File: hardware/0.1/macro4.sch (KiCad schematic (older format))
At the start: 22 parts, among them J1 USB_C_Receptacle_USB2.0, SW1 DFU, SW2 RST, SW3 SW_Push, SW5 SW_Push, SW6 SW_Push, SW7 Rotary_Encoder_MX, U1 AP2112K-3.3, U2 STM32F072C8Tx

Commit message: add RGB and silk to macro4
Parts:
- removed C6, C7: 100n, Capacitor_SMD:C_0603_1608Metric, symbol Device:C
- removed RN2: 10K, Resistor_SMD:R_Array_Convex_4x0603, symbol josh-passive:RN
- added D1, D2, D3: WS2812B, LED_SMD:LED_WS2812B_PLCC4_5.0x5.0mm_P3.2mm, symbol LED:WS2812B
- added Q1: BSS138, Package_TO_SOT_SMD:SOT-23, symbol Transistor_FET:BSS138
- added R1, R2: 10K, Resistor_SMD:R_0603_1608Metric_Pad1.05x0.95mm_HandSolder, symbol Device:R
- C1, C3: LCSC PN (none) -> C15849; MPN (none) -> CL10A105KB8NNNC
- C2, C4, C5: LCSC PN (none) -> C14663; MPN (none) -> CC0603KRX7R9BB104
- H1, H2, H3, H4, SW7: DNP (none) -> DNP
- J1: LCSC PN (none) -> C319148; MPN (none) -> U262-161N-4BVC11
- RN1: LCSC PN (none) -> C12028; MPN (none) -> 4D03WGJ0512T5E
- SW1, SW2: LCSC PN (none) -> C318936; MPN (none) -> TS-1101VS-C-A-A
- SW3, SW5, SW6: value SW_Push -> CHERRY_MX; DNP (none) -> DNP
- U1: LCSC PN (none) -> C51118; MPN (none) -> AP2112K-3.3TRG1
- U2: LCSC PN (none) -> C80488; MPN (none) -> STM32F072C8T6
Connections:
- net +3V3: now also Q1.1 (G), R1.1
- net ENC_A: now also SW7.A, U2.41 (PB5); no longer U2.42 (PB6)
- net ENC_B: now also SW7.B, U2.42 (PB6); no longer U2.41 (PB5)
- net GND: now also D1.3 (VSS), D2.3 (VSS), D3.3 (VSS)
- net VBUS: now also D1.1 (VDD), D2.1 (VDD), D3.1 (VDD), R2.1
- net LED: now reaches U2.25 (PB12)
- net LED: now also Q1.2 (S), R1.2
- new net: D1.2 (DOUT), D2.4 (DIN)
- new net: D1.4 (DIN), Q1.3 (D), R2.2
- new net: D2.2 (DOUT), D3.4 (DIN)
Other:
- note added: "Note: Encoder can be a MX switch or an encoder."
- note added: "Stopping ERC Errors"
- note removed: "Note: Encoder can be a MX switch or an encoder.\nOnly populate one!"
- note removed: "Stopping ERC"
- moved on the sheet: C2, H1, H2, H3, H4, RN1C, RN1D, SW1, SW2, SW7

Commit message: change buttons
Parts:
- SW1, SW2: footprint josh-buttons-switches:TL3330AF130QG -> josh-buttons-switches:Panasonic_EVQPUL_EVQPUC
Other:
- note added: "3v3 -> 5v logic shift"
- note added: "Addressable LEDs"
- moved on the sheet: D1, D2, D3, Q1, R1, R2, SW7

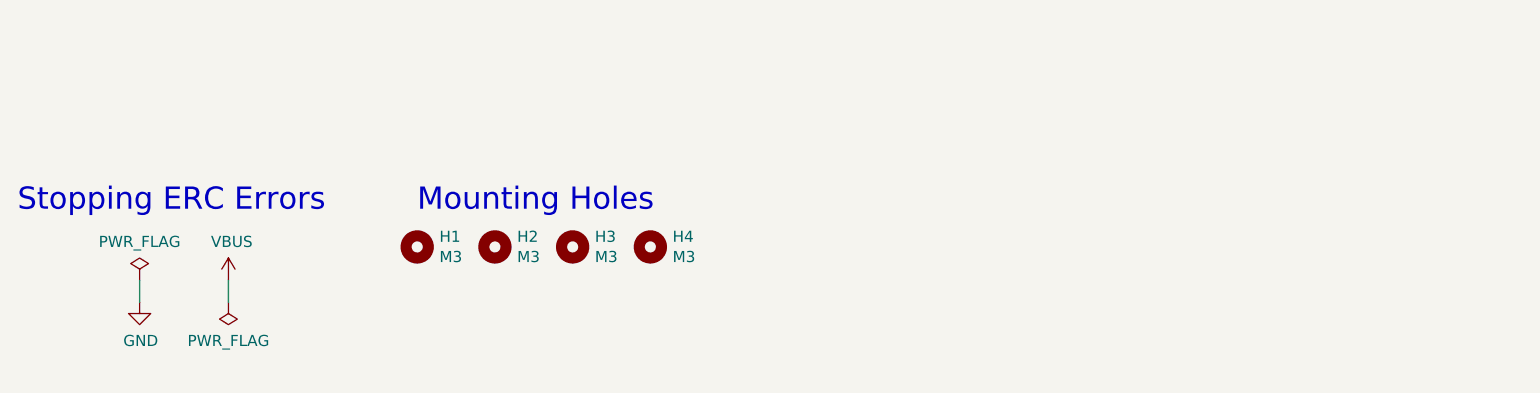
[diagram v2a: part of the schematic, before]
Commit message: update due to breaking lib change
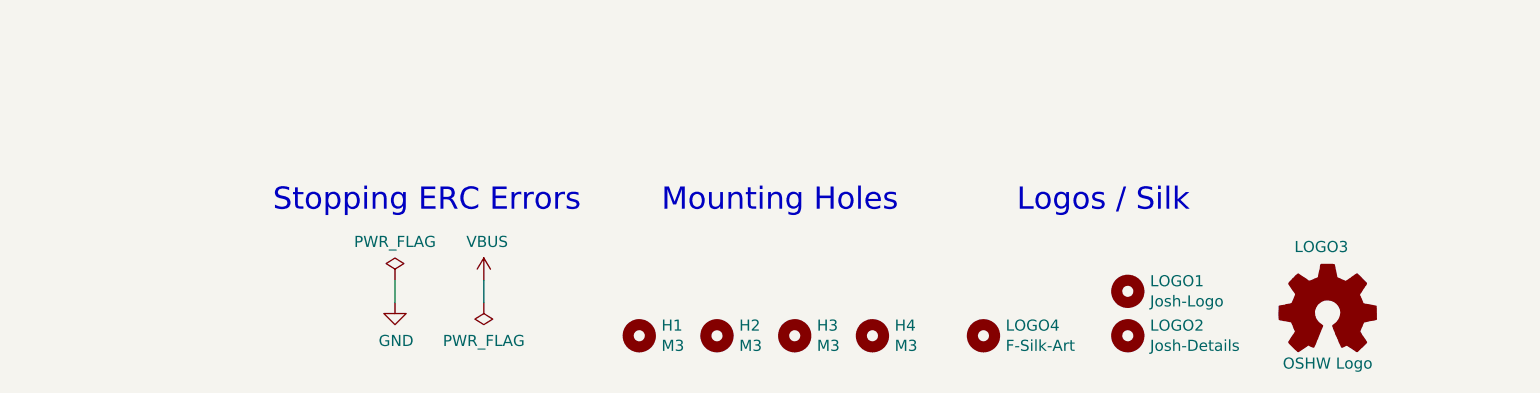
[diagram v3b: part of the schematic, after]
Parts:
- added LOGO1: Josh-Logo, josh-logos:josh-johnson-logo-11x2, symbol Mechanical:MountingHole
- added LOGO2: Josh-Details, josh-logos:josh-details, symbol Mechanical:MountingHole
- added LOGO3: OSHW Logo, josh-logos:OSHW_Logo_3.6x3.6_F.Mask, symbol Graphic:Logo_Open_Hardware_Small
- added LOGO4: F-Silk-Art, art:pattern_top, symbol Mechanical:MountingHole
- J1: footprint josh-connectors:USB_C_Receptacle_GT-USB-7010 -> josh-connectors:USB_C_U262-161N-4BVC11
- SW1, SW2: footprint josh-buttons-switches:Panasonic_EVQPUL_EVQPUC -> josh-buttons-switches:SW_Push_EVQPUL_EVQPUC
- SW3, SW5, SW6: footprint josh-buttons-switches:SW_Cherry_MX_1.00u_PCB -> josh-keyboard:MX_KEYSWITCH
- SW7: footprint josh-buttons-switches:MX_KEYSWITCH_ENCODER -> josh-keyboard:MX_KEYSWITCH_ENCODER
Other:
- note added: "Logos / Silk"
- moved on the sheet: H1, H2, H3, H4
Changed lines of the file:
@@
 F 0 "J1" H 950 3000 50  0000 C CNN
 F 1 "USB_C_Receptacle_USB2.0" H 1407 2926 50  0000 C CNN
-F 2 "josh-connectors:USB_C_Receptacle_GT-USB-7010" H 1450 2150 50  0001 C CNN
+F 2 "josh-connectors:USB_C_U262-161N-4BVC11" H 1450 2150 50  0001 C CNN
 F 3 "https://www.usb.org/sites/default/files/documents/usb_type-c.zip" H 1450 2150 50  0001 C CNN
 F 4 "C319148" H 1300 2150 50  0001 C CNN "LCSC PN"
@@
 F 0 "SW1" V 8696 3952 50  0000 R CNN
 F 1 "DFU" V 8605 3952 50  0000 R CNN
-F 2 "josh-buttons-switches:Panasonic_EVQPUL_EVQPUC" H 8650 4200 50  0001 C CNN
+F 2 "josh-buttons-switches:SW_Push_EVQPUL_EVQPUC" H 8650 4200 50  0001 C CNN
 F 3 "~" H 8650 4200 50  0001 C CNN
 F 4 "C318936" H 8650 4000 50  0001 C CNN "LCSC PN"
@@
 F 0 "SW2" V 9996 4402 50  0000 R CNN
 F 1 "RST" V 9905 4402 50  0000 R CNN
-F 2 "josh-buttons-switches:Panasonic_EVQPUL_EVQPUC" H 9950 4650 50  0001 C CNN
+F 2 "josh-buttons-switches:SW_Push_EVQPUL_EVQPUC" H 9950 4650 50  0001 C CNN
 F 3 "~" H 9950 4650 50  0001 C CNN
 F 4 "C318936" H 9950 4450 50  0001 C CNN "LCSC PN"
@@
 F 0 "SW7" H 9100 2367 50  0000 C CNN
 F 1 "Rotary_Encoder_MX" H 9100 2276 50  0000 C CNN
-F 2 "josh-buttons-switches:MX_KEYSWITCH_ENCODER" H 8950 2160 50  0001 C CNN
+F 2 "josh-keyboard:MX_KEYSWITCH_ENCODER" H 8950 2160 50  0001 C CNN
 F 3 "~" H 9100 2260 50  0001 C CNN
 F 4 "DNP" H 9100 2000 50  0001 C CNN "DNP"
@@
 F 0 "SW3" H 7600 2135 50  0000 C CNN
 F 1 "CHERRY_MX" H 7600 2044 50  0000 C CNN
-F 2 "josh-buttons-switches:SW_Cherry_MX_1.00u_PCB" H 7600 2050 50  0001 C CNN
+F 2 "josh-keyboard:MX_KEYSWITCH" H 7600 2050 50  0001 C CNN
 F 3 "~" H 7600 2050 50  0001 C CNN
 F 4 "DNP" H 7600 1850 50  0001 C CNN "DNP"
@@
 F 0 "SW5" H 7600 2535 50  0000 C CNN
 F 1 "CHERRY_MX" H 7600 2444 50  0000 C CNN
-F 2 "josh-buttons-switches:SW_Cherry_MX_1.00u_PCB" H 7600 2450 50  0001 C CNN
+F 2 "josh-keyboard:MX_KEYSWITCH" H 7600 2450 50  0001 C CNN
 F 3 "~" H 7600 2450 50  0001 C CNN
 F 4 "DNP" H 7600 2250 50  0001 C CNN "DNP"
@@
 F 0 "SW6" H 7600 2935 50  0000 C CNN
 F 1 "CHERRY_MX" H 7600 2844 50  0000 C CNN
-F 2 "josh-buttons-switches:SW_Cherry_MX_1.00u_PCB" H 7600 2850 50  0001 C CNN
+F 2 "josh-keyboard:MX_KEYSWITCH" H 7600 2850 50  0001 C CNN
 F 3 "~" H 7600 2850 50  0001 C CNN
 F 4 "DNP" H 7600 2650 50  0001 C CNN "DNP"
@@
 L Mechanical:MountingHole H1
 U 1 1 5E12347A
-P 2500 7200
-F 0 "H1" H 2600 7246 50  0000 L CNN
-F 1 "M3" H 2600 7155 50  0000 L CNN
-F 2 "MountingHole:MountingHole_3.2mm_M3" H 2500 7200 50  0001 C CNN
-F 3 "~" H 2500 7200 50  0001 C CNN
-F 4 "DNP" H 2500 7200 50  0001 C CNN "DNP"
-	1    2500 7200
+P 3500 7600
+F 0 "H1" H 3600 7646 50  0000 L CNN
+F 1 "M3" H 3600 7555 50  0000 L CNN
+F 2 "MountingHole:MountingHole_3.2mm_M3" H 3500 7600 50  0001 C CNN
+F 3 "~" H 3500 7600 50  0001 C CNN
+F 4 "DNP" H 3500 7600 50  0001 C CNN "DNP"
+	1    3500 7600
 	1    0    0    -1
 $EndComp
@@
 L Mechanical:MountingHole H3
 U 1 1 5E1240B9
-P 3200 7200
-F 0 "H3" H 3300 7246 50  0000 L CNN
-F 1 "M3" H 3300 7155 50  0000 L CNN
-F 2 "MountingHole:MountingHole_3.2mm_M3" H 3200 7200 50  0001 C CNN
-F 3 "~" H 3200 7200 50  0001 C CNN
-F 4 "DNP" H 3200 7200 50  0001 C CNN "DNP"
-	1    3200 7200
+P 4200 7600
+F 0 "H3" H 4300 7646 50  0000 L CNN
+F 1 "M3" H 4300 7555 50  0000 L CNN
+F 2 "MountingHole:MountingHole_3.2mm_M3" H 4200 7600 50  0001 C CNN
+F 3 "~" H 4200 7600 50  0001 C CNN
+F 4 "DNP" H 4200 7600 50  0001 C CNN "DNP"
+	1    4200 7600
 	1    0    0    -1
 $EndComp
@@
 L Mechanical:MountingHole H4
 U 1 1 5E127172
-P 3550 7200
-F 0 "H4" H 3650 7246 50  0000 L CNN
-F 1 "M3" H 3650 7155 50  0000 L CNN
-F 2 "MountingHole:MountingHole_3.2mm_M3" H 3550 7200 50  0001 C CNN
-F 3 "~" H 3550 7200 50  0001 C CNN
-F 4 "DNP" H 3550 7200 50  0001 C CNN "DNP"
-	1    3550 7200
+P 4550 7600
+F 0 "H4" H 4650 7646 50  0000 L CNN
+F 1 "M3" H 4650 7555 50  0000 L CNN
+F 2 "MountingHole:MountingHole_3.2mm_M3" H 4550 7600 50  0001 C CNN
+F 3 "~" H 4550 7600 50  0001 C CNN
+F 4 "DNP" H 4550 7600 50  0001 C CNN "DNP"
+	1    4550 7600
 	1    0    0    -1
 $EndComp
@@
 L Mechanical:MountingHole H2
 U 1 1 5E12A29E
-P 2850 7200
-F 0 "H2" H 2950 7246 50  0000 L CNN
-F 1 "M3" H 2950 7155 50  0000 L CNN
-F 2 "MountingHole:MountingHole_3.2mm_M3" H 2850 7200 50  0001 C CNN
-F 3 "~" H 2850 7200 50  0001 C CNN
-F 4 "DNP" H 2850 7200 50  0001 C CNN "DNP"
-	1    2850 7200
-	1    0    0    -1
-$EndComp
-Text Notes 2500 7050 0    100  ~ 0
+P 3850 7600
+F 0 "H2" H 3950 7646 50  0000 L CNN
+F 1 "M3" H 3950 7555 50  0000 L CNN
+F 2 "MountingHole:MountingHole_3.2mm_M3" H 3850 7600 50  0001 C CNN
+F 3 "~" H 3850 7600 50  0001 C CNN
+F 4 "DNP" H 3850 7600 50  0001 C CNN "DNP"
+	1    3850 7600
+	1    0    0    -1
+$EndComp
+Text Notes 3600 7050 0    100  ~ 0
 Mounting Holes
 Text Label 5100 3900 0    50   ~ 0
@@
 L power:PWR_FLAG #FLG0101
 U 1 1 5E2A8D8B
-P 1650 7450
-F 0 "#FLG0101" H 1650 7525 50  0001 C CNN
-F 1 "PWR_FLAG" H 1650 7623 50  0000 C CNN
-F 2 "" H 1650 7450 50  0001 C CNN
-F 3 "~" H 1650 7450 50  0001 C CNN
-	1    1650 7450
+P 2800 7450
+F 0 "#FLG0101" H 2800 7525 50  0001 C CNN
+F 1 "PWR_FLAG" H 2800 7623 50  0000 C CNN
+F 2 "" H 2800 7450 50  0001 C CNN
+F 3 "~" H 2800 7450 50  0001 C CNN
+	1    2800 7450
 	-1   0    0    1
 $EndComp
@@
 L power:VBUS #PWR0101
 U 1 1 5E2A941E
-P 1650 7350
-F 0 "#PWR0101" H 1650 7200 50  0001 C CNN
-F 1 "VBUS" H 1665 7523 50  0000 C CNN
-F 2 "" H 1650 7350 50  0001 C CNN
-F 3 "" H 1650 7350 50  0001 C CNN
-	1    1650 7350
-	1    0    0    -1
-$EndComp
-Wire Wire Line
-	1650 7450 1650 7350
+P 2800 7350
+F 0 "#PWR0101" H 2800 7200 50  0001 C CNN
+F 1 "VBUS" H 2815 7523 50  0000 C CNN
+F 2 "" H 2800 7350 50  0001 C CNN
+F 3 "" H 2800 7350 50  0001 C CNN
+	1    2800 7350
+	1    0    0    -1
+$EndComp
+Wire Wire Line
+	2800 7450 2800 7350
 $Comp
 L power:PWR_FLAG #FLG0102
 U 1 1 5E2C6A4F
-P 1250 7350
-F 0 "#FLG0102" H 1250 7425 50  0001 C CNN
-F 1 "PWR_FLAG" H 1250 7523 50  0000 C CNN
-F 2 "" H 1250 7350 50  0001 C CNN
-F 3 "~" H 1250 7350 50  0001 C CNN
-	1    1250 7350
-	1    0    0    -1
-$EndComp
-Wire Wire Line
-	1250 7350 1250 7450
+P 2400 7350
+F 0 "#FLG0102" H 2400 7425 50  0001 C CNN
+F 1 "PWR_FLAG" H 2400 7523 50  0000 C CNN
+F 2 "" H 2400 7350 50  0001 C CNN
+F 3 "~" H 2400 7350 50  0001 C CNN
+	1    2400 7350
+	1    0    0    -1
+$EndComp
+Wire Wire Line
+	2400 7350 2400 7450
 $Comp
 L power:GND #PWR0102
 U 1 1 5E2CDE1D
-P 1250 7450
-F 0 "#PWR0102" H 1250 7200 50  0001 C CNN
-F 1 "GND" H 1255 7277 50  0000 C CNN
-F 2 "" H 1250 7450 50  0001 C CNN
-F 3 "" H 1250 7450 50  0001 C CNN
-	1    1250 7450
-	1    0    0    -1
-$EndComp
-Text Notes 700  7050 0    100  ~ 0
+P 2400 7450
+F 0 "#PWR0102" H 2400 7200 50  0001 C CNN
+F 1 "GND" H 2405 7277 50  0000 C CNN
+F 2 "" H 2400 7450 50  0001 C CNN
+F 3 "" H 2400 7450 50  0001 C CNN
+	1    2400 7450
+	1    0    0    -1
+$EndComp
+Text Notes 1850 7050 0    100  ~ 0
 Stopping ERC Errors
 Wire Wire Line
@@
 Text Notes 1350 5100 0    50   ~ 0
 3v3 -> 5v logic shift
+$Comp
+L Graphic:Logo_Open_Hardware_Small LOGO3
+U 1 1 5E2DDC16
+P 6600 7500
+F 0 "LOGO3" H 6450 7800 50  0000 L CNN
+F 1 "OSHW Logo" H 6600 7275 50  0000 C CNN
+F 2 "josh-logos:OSHW_Logo_3.6x3.6_F.Mask" H 6600 7500 50  0001 C CNN
+F 3 "~" H 6600 7500 50  0001 C CNN
+	1    6600 7500
+	1    0    0    -1
+$EndComp
+$Comp
+L Mechanical:MountingHole LOGO2
+U 1 1 5E2DE9EF
+P 5700 7600
+F 0 "LOGO2" H 5800 7646 50  0000 L CNN
+F 1 "Josh-Details" H 5800 7555 50  0000 L CNN
+F 2 "josh-logos:josh-details" H 5700 7600 50  0001 C CNN
+F 3 "~" H 5700 7600 50  0001 C CNN
+	1    5700 7600
+	1    0    0    -1
+$EndComp
+$Comp
+L Mechanical:MountingHole LOGO1
+U 1 1 5E2DEB8C
+P 5700 7400
+F 0 "LOGO1" H 5800 7446 50  0000 L CNN
+F 1 "Josh-Logo" H 5800 7355 50  0000 L CNN
+F 2 "josh-logos:josh-johnson-logo-11x2" H 5700 7400 50  0001 C CNN
+F 3 "~" H 5700 7400 50  0001 C CNN
+	1    5700 7400
+	1    0    0    -1
+$EndComp
+Text Notes 5200 7050 0    100  ~ 0
+Logos / Silk
+$Comp
+L Mechanical:MountingHole LOGO4
+U 1 1 5E2F0EBE
+P 5050 7600
+F 0 "LOGO4" H 5150 7646 50  0000 L CNN
+F 1 "F-Silk-Art" H 5150 7555 50  0000 L CNN
+F 2 "art:pattern_top" H 5050 7600 50  0001 C CNN
+F 3 "~" H 5050 7600 50  0001 C CNN
+	1    5050 7600
+	1    0    0    -1
+$EndComp
 $EndSCHEMATC

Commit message: v0.2
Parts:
- C1, C3: DigiKey (none) -> 1276-1866-1-ND; LCSC (none) -> C15849; LCSC PN C15849 -> (none); MPN CL10A105KB8NNNC -> CL10A105MP8NNNC; Manufacturer (none) -> Samsung Electro-Mechanics
- C2, C4, C5: DigiKey (none) -> 1276-1000-1-ND; LCSC (none) -> C14663; LCSC PN C14663 -> (none); MPN CC0603KRX7R9BB104 -> CL10B104KB8NNNC; Manufacturer (none) -> Samsung Electro-Mechanics
- D1, D2, D3: DigiKey (none) -> 1528-1104-ND; LCSC (none) -> C114586; MPN (none) -> WS2812B-B; Manufacturer (none) -> Worldsemi; Notes (none) -> Digikey PN Quantity 10
- J1: LCSC (none) -> C319148; LCSC PN C319148 -> (none); Manufacturer (none) -> XKB Enterprise; Notes (none) -> Not avail from DigiKey
- LOGO1, LOGO2, LOGO3, LOGO4: DNP (none) -> DNP
- Q1: DigiKey (none) -> 1727-1142-1-ND; LCSC (none) -> C75547; MPN (none) -> BSS138P,215; Manufacturer (none) -> Nexperia
- R1, R2: DigiKey (none) -> CR0603-JW-103ELFCT-ND; LCSC (none) -> C144116; MPN (none) -> CR0603-JW-103ELF; Manufacturer (none) -> Bourns; Notes (none) -> LCSC PN Sub
- RN1: DigiKey (none) -> CAY16-512J4LFCT-ND; LCSC (none) -> C12028; LCSC PN C12028 -> (none); MPN 4D03WGJ0512T5E -> CAY16-512J4LF; Manufacturer (none) -> Bourns; Notes (none) -> LCSC PN Sub
- SW1: value DFU -> PTS840; footprint josh-buttons-switches:SW_Push_EVQPUL_EVQPUC -> josh-buttons-switches:SW_Push_PTS840; DigiKey (none) -> CKN10884CT-ND; LCSC (none) -> C221909; LCSC PN C318936 -> (none); MPN TS-1101VS-C-A-A -> PTS840GMSMTRLFS; Manufacturer (none) -> C&K; Name (none) -> DFU; Notes (none) -> Substutite okay
- SW2: value RST -> PTS840; footprint josh-buttons-switches:SW_Push_EVQPUL_EVQPUC -> josh-buttons-switches:SW_Push_PTS840; DigiKey (none) -> CKN10884CT-ND; LCSC (none) -> C221909; LCSC PN C318936 -> (none); MPN TS-1101VS-C-A-A -> PTS840GMSMTRLFS; Manufacturer (none) -> C&K; Name (none) -> RST; Notes (none) -> Substutite okay
- U1: DigiKey (none) -> AP2112K-3.3TRG1DICT-ND; LCSC (none) -> C51118; LCSC PN C51118 -> (none); Manufacturer (none) -> Diodes Inc
- U2: DigiKey (none) -> 497-17358-ND; LCSC (none) -> C80488; LCSC PN C80488 -> (none); Manufacturer (none) -> STMicroelectronics
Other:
- moved on the sheet: RN1C
